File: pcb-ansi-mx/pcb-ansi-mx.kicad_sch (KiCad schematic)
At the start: 200 parts, among them J1 USB_C_Receptacle_USB2.0, J2 Conn_01x04, J3 Conn_01x05, SW1 SW_Push, SW2 SW_Push, U1 XC6206PxxxMR, U2 SRV05-4, U3 RP2040, U4 W25Q128JVS, Y1 Crystal_GND24

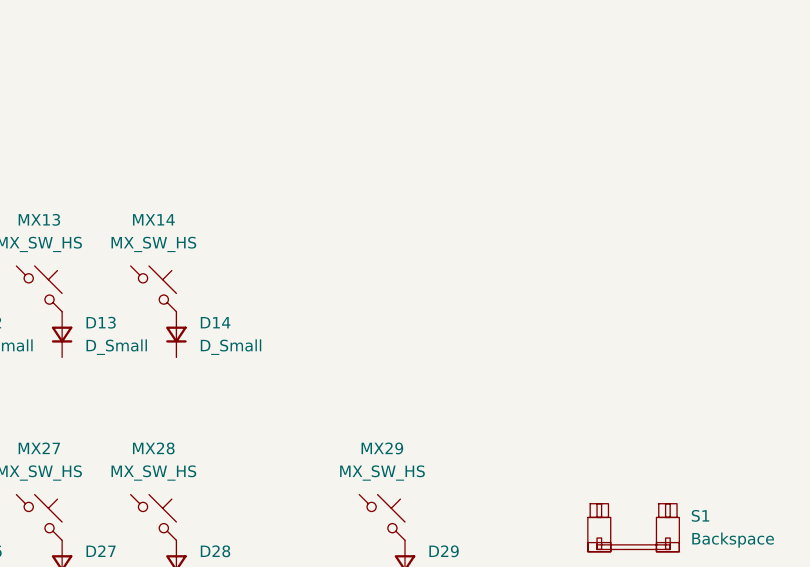
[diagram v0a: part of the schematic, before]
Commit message: feat: add rotary encoder
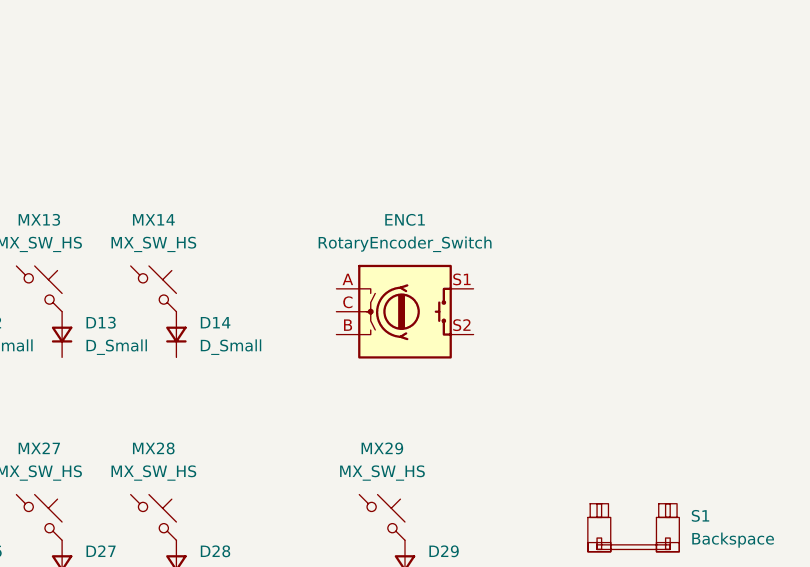
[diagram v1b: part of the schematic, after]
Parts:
- added ENC1: RotaryEncoder_Switch, PCM_marbastlib-various:ROT_Alps_EC11E-Switch, symbol Device:RotaryEncoder_Switch
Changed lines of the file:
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@@
+    )
+  )
+  (symbol (lib_id "Device:RotaryEncoder_Switch") (at 353.06 124.46 0) (unit 1)
+    (in_bom yes) (on_board yes) (dnp no) (fields_autoplaced)
+    (property "Reference" "ENC1" (at 353.06 114.3 0)
+      (effects (font (size 1.27 1.27)))
+    )
+    (property "Value" "RotaryEncoder_Switch" (at 353.06 116.84 0)
+      (effects (font (size 1.27 1.27)))
+    )
+    (property "Footprint" "PCM_marbastlib-various:ROT_Alps_EC11E-Switch" (at 349.25 120.396 0)
+      (effects (font (size 1.27 1.27)) hide)
+    )
+    (property "Datasheet" "~" (at 353.06 117.856 0)
+      (effects (font (size 1.27 1.27)) hide)
+    )
+    (pin "A")
+    (pin "B")
+    (pin "C")
+    (pin "S1")
+    (pin "S2")
+    (instances
+      (project "pcb-ansi-mx"
+        (path "/3f8b7912-237d-49db-8468-ce09efba1abe"
+          (reference "ENC1") (unit 1)
+        )
+      )
     )
   )

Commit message: feat: initial key matrix + encoder debounce
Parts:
- added C10, C11: 10n, Capacitor_SMD:C_0402_1005Metric, symbol Device:C_Small
- added D_ENC1: D_Small, Diode_SMD:D_SOD-123, symbol Device:D_Small
- added R10, R7, R8, R9: 5k1, Resistor_SMD:R_0402_1005Metric, symbol Device:R_Small
- renumbered C10 to C12, C11 to C13, C12 to C14, R7 to R11, R8 to R12, R9 to R13, S3 to S1, S4 to S2, S1 to S3, S2 to S4
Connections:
- net GND: now also ENC1.C, C10.2, C11.2
- net ROW5: now reaches D75.1 (K)
- net ROW5: now also D73.1 (K), D74.1 (K), D76.1 (K), D77.1 (K), D78.1 (K), D79.1 (K), D80.1 (K), D81.1 (K), D82.1 (K)
- net ROW1: now reaches D23.1 (K)
- net ROW1: now also D15.1 (K), D16.1 (K), D17.1 (K), D18.1 (K), D19.1 (K), D20.1 (K), D21.1 (K), D22.1 (K), D24.1 (K), D25.1 (K), D26.1 (K), D27.1 (K), D28.1 (K), D29.1 (K)
- net COL11: now reaches MX80.1
- net COL11: now also MX12.1, MX26.1, MX41.1, MX56.1, MX70.1
- net ROW0: now reaches D12.1 (K)
- net ROW0: now also D1.1 (K), D10.1 (K), D11.1 (K), D13.1 (K), D14.1 (K), D2.1 (K), D3.1 (K), D4.1 (K), D5.1 (K), D6.1 (K), D7.1 (K), D8.1 (K), D9.1 (K), D_ENC1.1 (K)
- net COL4: now reaches MX63.1
- net COL4: now also MX19.1, MX34.1, MX49.1, MX5.1
- net ROW4: now reaches D61.1 (K)
- net ROW4: now also D59.1 (K), D60.1 (K), D62.1 (K), D63.1 (K), D64.1 (K), D65.1 (K), D66.1 (K), D67.1 (K), D68.1 (K), D69.1 (K), D70.1 (K), D71.1 (K), D72.1 (K)
- net COL6: now reaches MX65.1
- net COL6: now also MX21.1, MX36.1, MX51.1, MX7.1
- net COL0: now reaches MX45.1
- net COL0: now also MX1.1, MX15.1, MX30.1, MX59.1, MX73.1
- net ROW2: now reaches D32.1 (K)
- net ROW2: now also D30.1 (K), D31.1 (K), D33.1 (K), D34.1 (K), D35.1 (K), D36.1 (K), D37.1 (K), D38.1 (K), D39.1 (K), D40.1 (K), D41.1 (K), D42.1 (K), D43.1 (K), D44.1 (K)
- net COL9: now reaches MX24.1
- net COL9: now also MX10.1, MX39.1, MX54.1, MX68.1, MX78.1
- net ROW3: now reaches D54.1 (K)
- net ROW3: now also D45.1 (K), D46.1 (K), D47.1 (K), D48.1 (K), D49.1 (K), D50.1 (K), D51.1 (K), D52.1 (K), D53.1 (K), D55.1 (K), D56.1 (K), D57.1 (K), D58.1 (K)
- net COL14: now reaches MX44.1
- net COL14: now also ENC1.S2, MX29.1, MX58.1, MX72.1
- net COL5: now reaches MX64.1
- net COL5: now also MX20.1, MX35.1, MX50.1, MX6.1, MX76.1
- net at ENC1.A: now also R7.2
- net at ENC1.B: now also R9.2
- net at ENC1.S1: now also D_ENC1.2 (A)
- net COL10: now reaches MX40.1
- net COL10: now also MX11.1, MX25.1, MX55.1, MX69.1, MX79.1
- net COL12: now reaches MX71.1
- net COL12: now also MX13.1, MX27.1, MX42.1, MX57.1, MX81.1
- net COL1: now reaches MX31.1
- net COL1: now also MX16.1, MX2.1, MX46.1, MX60.1, MX74.1
- net COL2: now reaches MX32.1
- net COL2: now also MX17.1, MX3.1, MX47.1, MX61.1, MX75.1
- net COL3: now reaches MX33.1
- net COL3: now also MX18.1, MX4.1, MX48.1, MX62.1
- net COL8: now reaches MX23.1
- net COL8: now also MX38.1, MX53.1, MX67.1, MX77.1, MX9.1
- net COL13: now reaches MX14.1
- net COL13: now also MX28.1, MX43.1, MX82.1
- net COL7: now reaches MX37.1
- net COL7: now also MX22.1, MX52.1, MX66.1, MX8.1
- new net: R10.2, R9.1
- new net: R7.1, R8.2
- new net ENC_A: C11.1, R8.1
- new net ENC_B: C10.1, R10.1
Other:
- moved on the sheet: D1, D10, D11, D12, D13, D14, D15, D16, D17, D18, D19, D2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

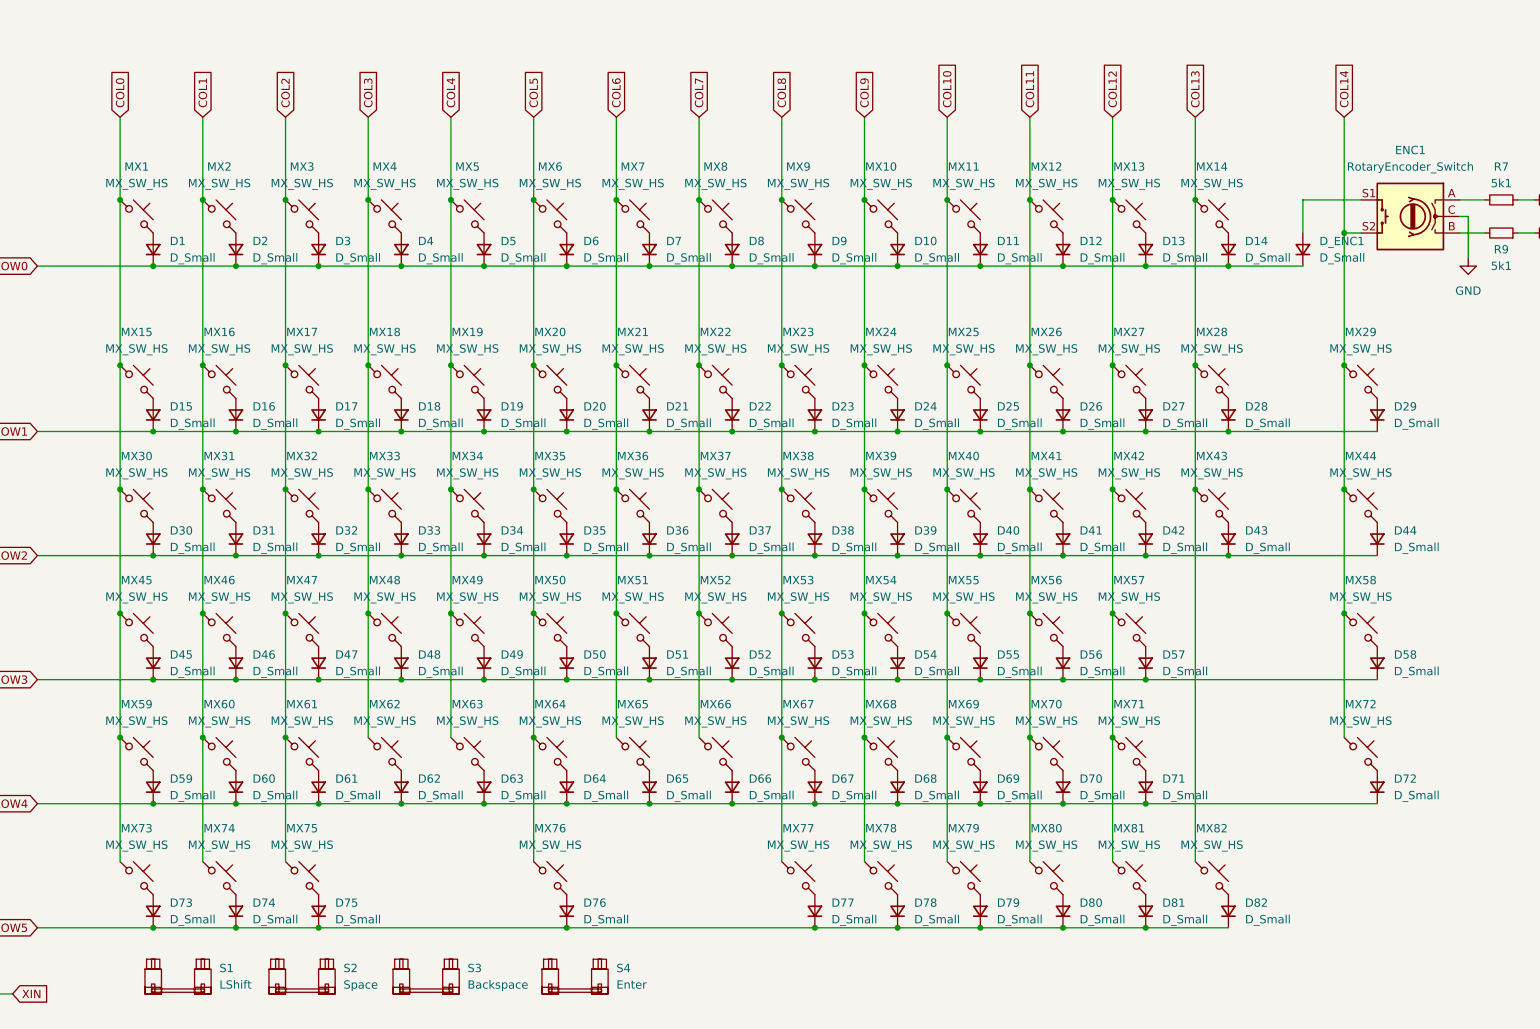
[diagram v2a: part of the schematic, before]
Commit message: refactor: remove f13 (to make space for usb port)
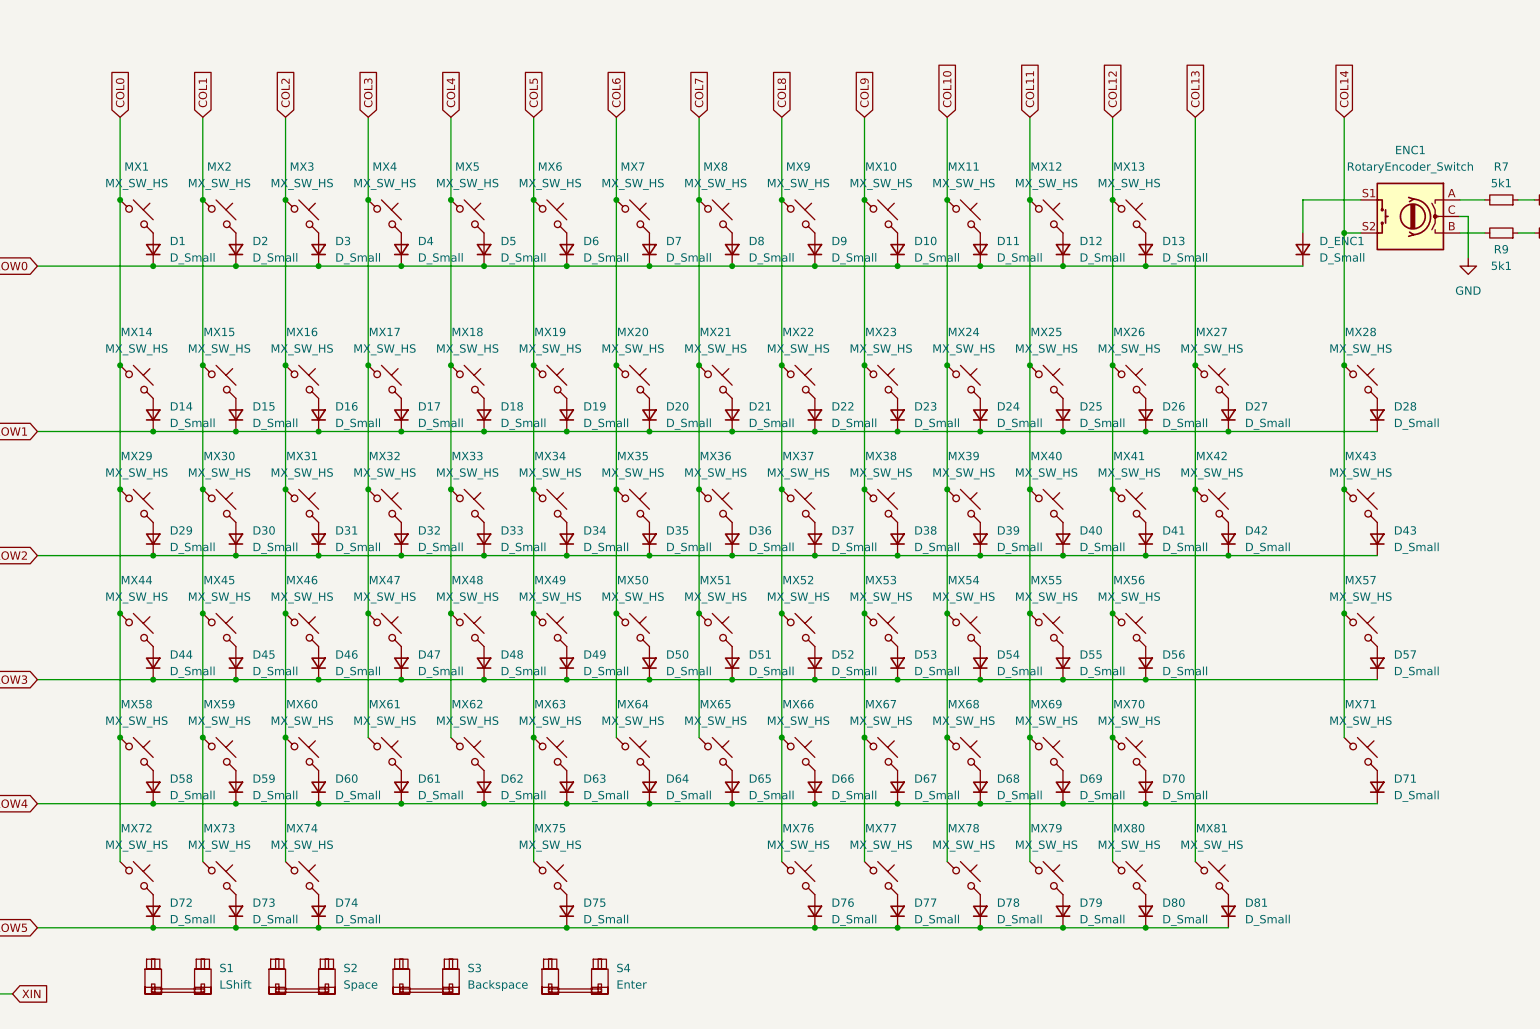
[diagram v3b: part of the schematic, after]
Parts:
- removed D14: D_Small, Diode_SMD:D_SOD-123, symbol Device:D_Small
- removed MX14: MX_SW_HS, PCM_marbastlib-mx:SW_MX_HS_1u, symbol PCM_marbastlib-mx:MX_SW_HS
- renumbered D15 to D14, D16 to D15, D17 to D16, D18 to D17, D19 to D18, D20 to D19, D21 to D20, D22 to D21, D23 to D22, D24 to D23, D25 to D24, D26 to D25, D27 to D26, D28 to D27, D29 to D28, D30 to D29, D31 to D30, D32 to D31, D33 to D32, D34 to D33, D35 to D34, D36 to D35, D37 to D36, D38 to D37, D39 to D38, D40 to D39, D41 to D40, D42 to D41, D43 to D42, D44 to D43, D45 to D44, D46 to D45, D47 to D46, D48 to D47, D49 to D48, D50 to D49, D51 to D50, D52 to D51, D53 to D52, D54 to D53, D55 to D54, D56 to D55, D57 to D56, D58 to D57, D59 to D58, D60 to D59, D61 to D60, D62 to D61, D63 to D62, D64 to D63, D65 to D64, D66 to D65, D67 to D66, D68 to D67, D69 to D68, D70 to D69, D71 to D70, D72 to D71, D73 to D72, D74 to D73, D75 to D74, D76 to D75, D77 to D76, D78 to D77, D79 to D78, D80 to D79, D81 to D80, D82 to D81, MX15 to MX14, MX16 to MX15, MX17 to MX16, MX18 to MX17, MX19 to MX18, MX20 to MX19, MX21 to MX20, MX22 to MX21, MX23 to MX22, MX24 to MX23, MX25 to MX24, MX26 to MX25, MX27 to MX26, MX28 to MX27, MX29 to MX28, MX30 to MX29, MX31 to MX30, MX32 to MX31, MX33 to MX32, MX34 to MX33, MX35 to MX34, MX36 to MX35, MX37 to MX36, MX38 to MX37, MX39 to MX38, MX40 to MX39, MX41 to MX40, MX42 to MX41, MX43 to MX42, MX44 to MX43, MX45 to MX44, MX46 to MX45, MX47 to MX46, MX48 to MX47, MX49 to MX48, MX50 to MX49, MX51 to MX50, MX52 to MX51, MX53 to MX52, MX54 to MX53, MX55 to MX54, MX56 to MX55, MX57 to MX56, MX58 to MX57, MX59 to MX58, MX60 to MX59, MX61 to MX60, MX62 to MX61, MX63 to MX62, MX64 to MX63, MX65 to MX64, MX66 to MX65, MX67 to MX66, MX68 to MX67, MX69 to MX68, MX70 to MX69, MX71 to MX70, MX72 to MX71, MX73 to MX72, MX74 to MX73, MX75 to MX74, MX76 to MX75, MX77 to MX76, MX78 to MX77, MX79 to MX78, MX80 to MX79, MX81 to MX80, MX82 to MX81

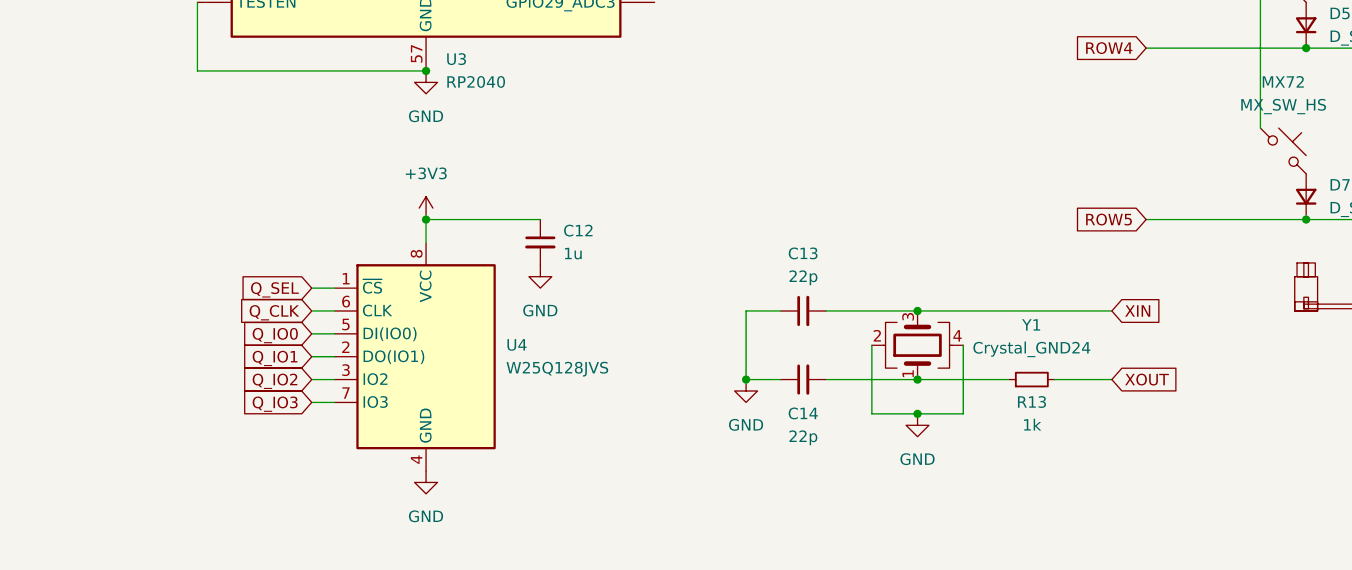
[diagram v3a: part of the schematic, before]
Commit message: refactor: use molex instead of jst for daughterboard connector
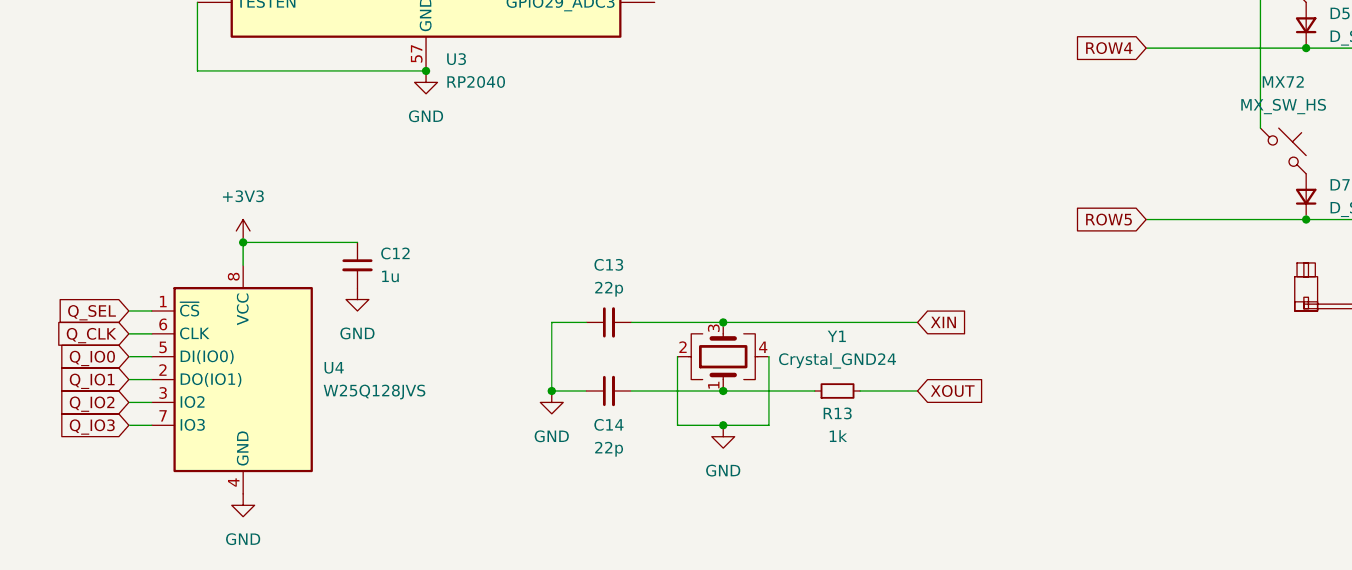
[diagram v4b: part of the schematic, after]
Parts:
- J2: footprint Connector_JST:JST_SH_SM04B-SRSS-TB_1x04-1MP_P1.00mm_Horizontal -> Connector_Molex:Molex_Pico-EZmate_78171-0004_1x04-1MP_P1.20mm_Vertical
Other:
- moved on the sheet: C12, C13, C14, R13, U4, Y1

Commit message: refactor: remove daughterboard connector
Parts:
- removed J2: Conn_01x04, Connector_Molex:Molex_Pico-EZmate_78171-0004_1x04-1MP_P1.20mm_Vertical, symbol Connector_Generic:Conn_01x04
- added C11, C12, C13, C5: 100n, Capacitor_SMD:C_0402_1005Metric, symbol Device:C_Small
- renumbered C9 to C10, C10 to C14, C11 to C15, C12 to C16, C13 to C17, C14 to C18, C5 to C6, C6 to C7, C7 to C8, C8 to C9
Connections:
- net +1V1: now also C5.1
- net +3V3: now also C11.1, C12.1, C13.1
- net GND: now also C11.2, C12.2, C13.2, C5.2
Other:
- moved on the sheet: C10, C3, C4, C6, C7, C8, C9, J3, R3, R4, R5, R6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
